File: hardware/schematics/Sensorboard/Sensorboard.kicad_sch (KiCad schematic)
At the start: 36 parts, among them J1 Grauwasser, J2 BNO055 IMU, J3 BME680 #0 Innen, J4 RS485, J5 BME680 #1 Außen, J6 HX711 GasWaage, J7 LT452 Malibu, J8 Frischwasser, U1 ESP32-S3-DevKitC, U2 TSR1-2450E, U3 MCP1700x-330xxTT, U4 SP3485CP, U5 PCF8523T, Y1 32.768

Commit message: hw(sensorboard): KiCad Schaltplan aktualisiert, Gerber + Fertigungsdaten Rev 1.0
- Sensorboard KiCad-Dateien aktualisiert (PCB, Schaltplan, Projekt)
- Autosave-/Lock-Dateien entfernt
- Gerber-Dateien für alle Layer hinzugefügt
- Fertigungspaket Rev 1.0 (BOM, Bestückung, Positionen, IPC-Netlist)
- Interactive BOM (ibom.html) hinzugefügt
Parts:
- removed U2: TSR1-2450E, Converter_DCDC:Converter_DCDC_TRACO_TSR1-xxxxE_THT, symbol Converter_DCDC:TSR1-2450E
- removed U3: MCP1700x-330xxTT, Package_TO_SOT_SMD:SOT-23, symbol Regulator_Linear:MCP1700x-330xxTT
- added D5, D6, D7: 1N4148, Diode_THT:D_DO-35_SOD27_P7.62mm_Horizontal, symbol Diode:1N4148
- added D8, D9: BZV55B3V3, Diode_SMD:D_MiniMELF, symbol Diode:BZV55B3V3
- added H1, H2, H3, H4: MountingHole_Pad, MountingHole:MountingHole_3.2mm_M3_Pad, symbol Mechanical:MountingHole_Pad
- added Q1, Q2, Q3: BSS138, Package_TO_SOT_SMD:SOT-23, symbol Transistor_FET:BSS138
- added R11, R13, R15: 100, Resistor_SMD:R_0402_1005Metric, symbol Device:R
- added R12, R14, R16, R17, R19: 100k, Resistor_SMD:R_0402_1005Metric, symbol Device:R
- added R18, R20: 22k, Resistor_SMD:R_0402_1005Metric, symbol Device:R
- added TP1: USB PWR, Connector_PinHeader_2.54mm:PinHeader_1x02_P2.54mm_Vertical, symbol Connector:TestPoint_2Pole
- added U2: TSR2-2450, Converter_DCDC:Converter_DCDC_TRACO_TSR2-xxxx_THT, symbol Converter_DCDC:TSR2-2450
- added U3: LDL1117S33R, Package_TO_SOT_SMD:SOT-223-3_TabPin2, symbol Regulator_Linear:AMS1117-3.3
- C1, C2: footprint (none) -> Capacitor_THT:CP_Radial_D5.0mm_P2.50mm
- C3, C4: value 1uF -> 10uF; footprint (none) -> Capacitor_SMD:C_0402_1005Metric
- C5, C6: footprint (none) -> Capacitor_SMD:C_0402_1005Metric
- J1, J8: footprint (none) -> Connector_JST:JST_XH_B3B-XH-A_1x03_P2.50mm_Vertical
- NT1: footprint (none) -> NetTie:NetTie-2_SMD_Pad0.5mm
- R1, R10, R2, R3, R4, R5, R6, R7, R8, R9: footprint (none) -> Resistor_SMD:R_0402_1005Metric
- Y1: footprint (none) -> Crystal:Crystal_SMD_3215-2Pin_3.2x1.5mm
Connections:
- net +3.3V: now also U3.2 (VO)
- net +5V: now also U2.3 (Vout), U3.3 (VI)
- net 12V - AUS: now also D6.2 (A), Q2.3 (D)
- net 12V - EIN: now also D5.2 (A), Q1.3 (D)
- net GND: now also D8.2 (A), D9.2 (A), H1.1, H2.1, H3.1, H4.1, Q1.2 (S), Q2.2 (S), Q3.2 (S), R12.1, R14.1, R16.1, R18.2, R20.2, TP1.1, U2.2 (GND), U3.1 (GND)
- net Multimedia: now also D7.2 (A), Q3.3 (D)
- net SB: now also R17.1
- net at U1.17 (GPIO11/ADC2_CH0): now also R11.1
- net at U1.18 (GPIO12/ADC2_CH1): now also R13.1
- net at U1.19 (GPIO13/ADC2_CH2): now also R15.1
- net at U1.4 (GPIO4/ADC1_CH3): now also D8.1 (K), R17.2, R18.1
- net at U1.5 (GPIO5/ADC1_CH4): now also D9.1 (K), R19.2, R20.1
- net +12V renamed WB
- net WB: now also D5.1 (K), D6.1 (K), D7.1 (K), R19.1, TP1.2, U2.1 (Vin)
- new net: Q2.1 (G), R13.2, R14.2
- new net: Q1.1 (G), R11.2, R12.2
- new net: Q3.1 (G), R15.2, R16.2
- no-connect marks 4 -> 27
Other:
- moved on the sheet: D4

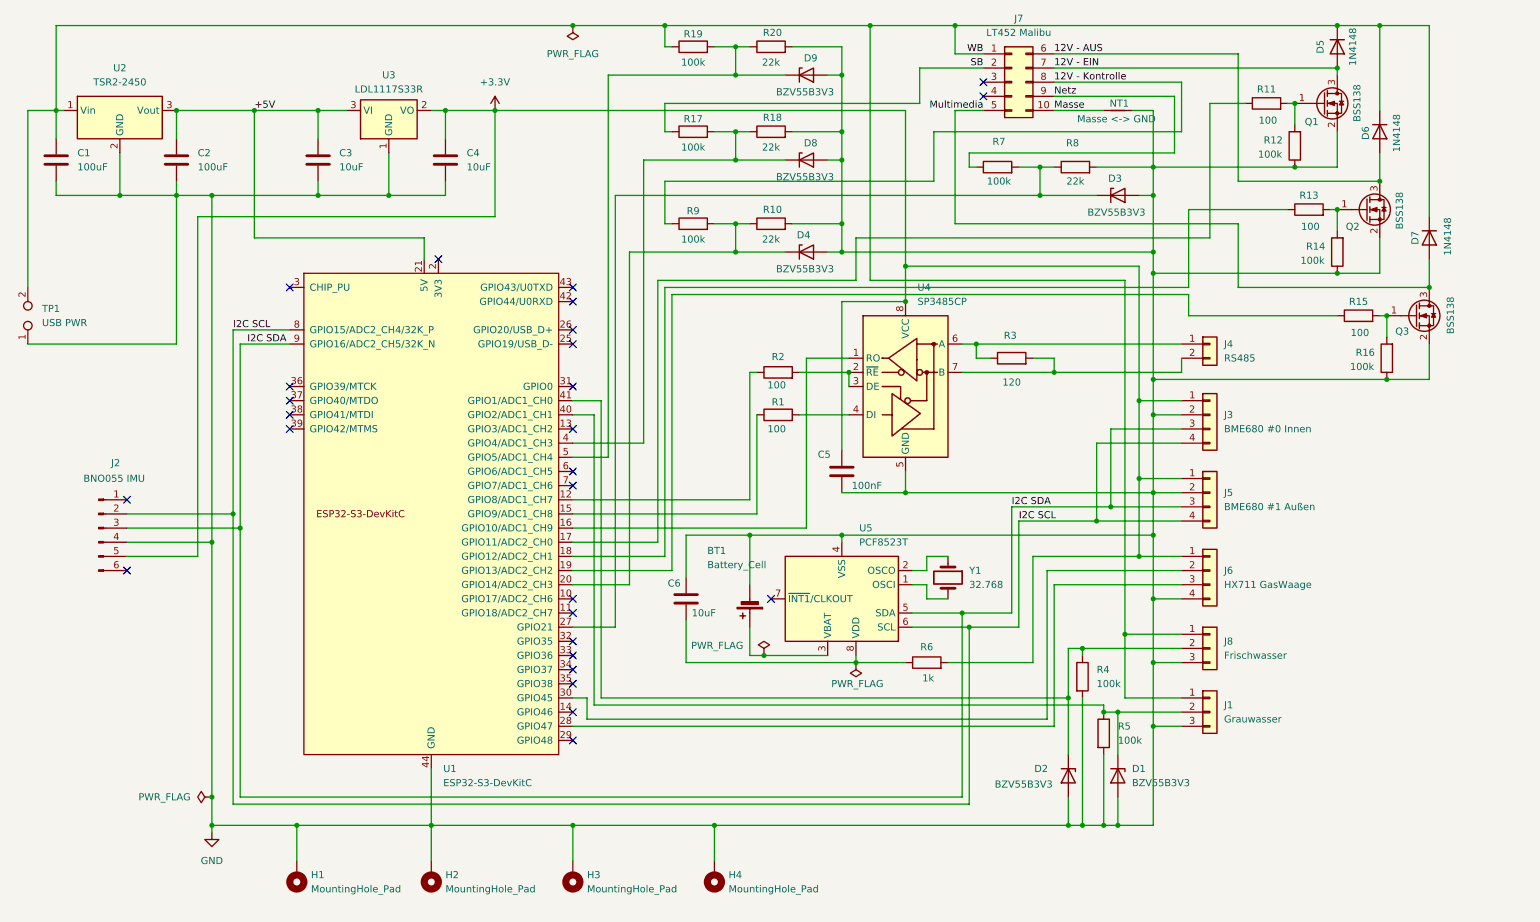
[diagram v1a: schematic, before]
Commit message: hw(sensorboard): KiCad Schaltplan + Gerber aktualisiert
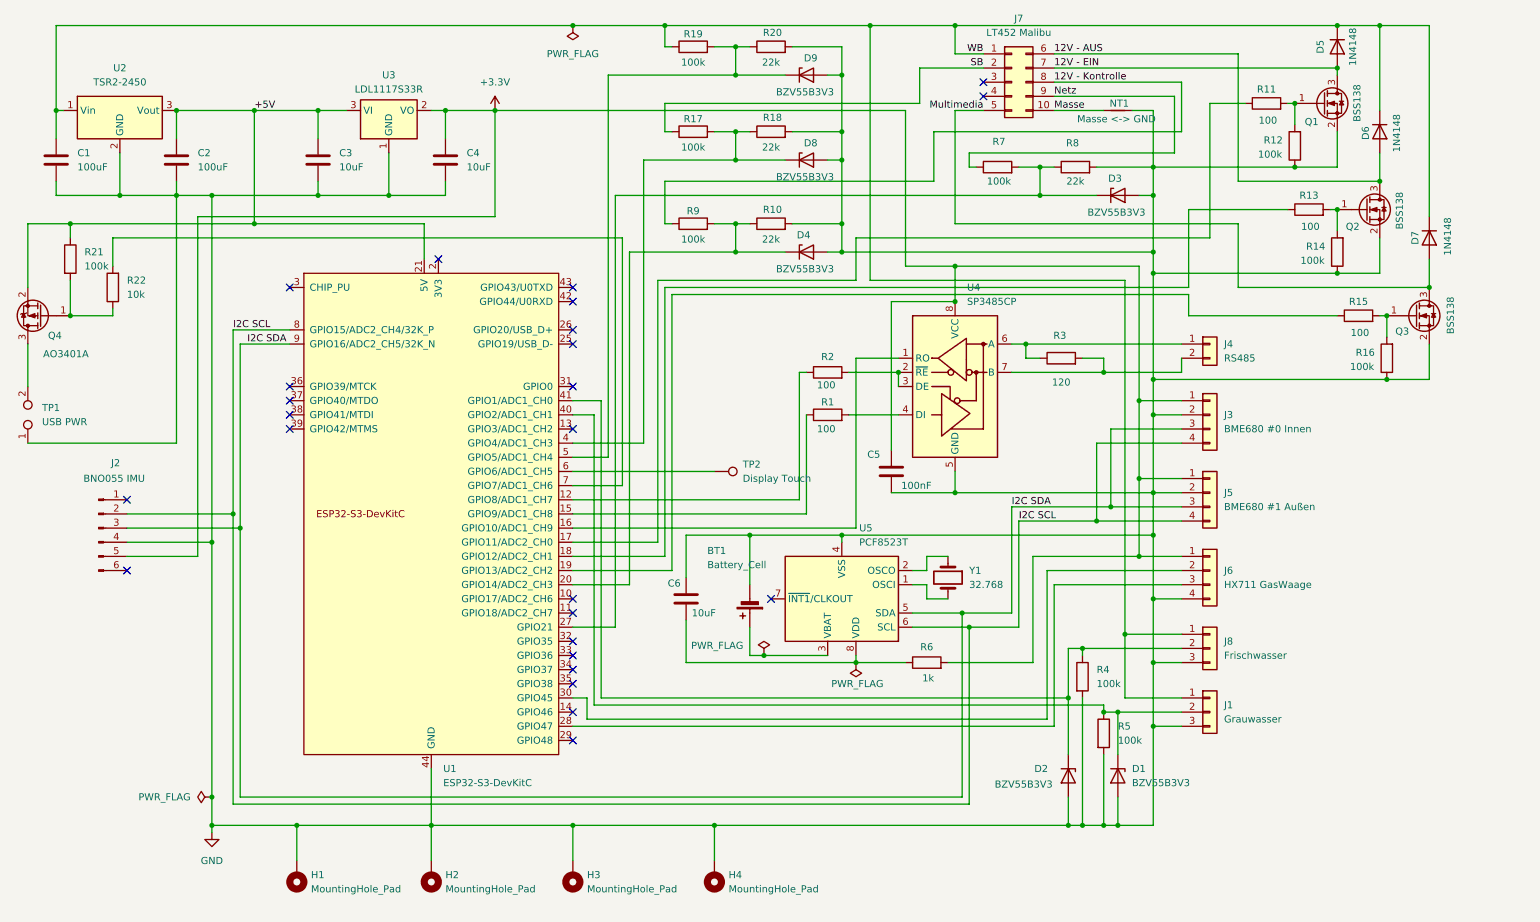
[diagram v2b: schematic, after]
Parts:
- added Q4: AO3401A, Package_TO_SOT_SMD:SOT-23, symbol Transistor_FET:AO3401A
- added R21: 100k, Resistor_SMD:R_0402_1005Metric, symbol Device:R
- added R22: 10k, Resistor_SMD:R_0402_1005Metric, symbol Device:R
- added TP2: Display Touch, TestPoint:TestPoint_THTPad_1.0x1.0mm_Drill0.5mm, symbol Connector:TestPoint
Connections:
- net +5V: now also Q4.2 (S), R21.1
- net WB: no longer TP1.2
- net at U1.6 (GPIO6/ADC1_CH5): now also TP2.1
- net at U1.7 (GPIO7/ADC1_CH6): now also R22.2
- new net: Q4.1 (G), R21.2, R22.1
- new net: Q4.3 (D), TP1.2
- no-connect marks 27 -> 25
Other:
- moved on the sheet: C5, R1, R2, R3, TP1, U4

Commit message: hardware(kicad): Sensorboard Rev 1.0 – Schematic/PCB aktualisiert, Produktionsdateien aus Tracking entfernt
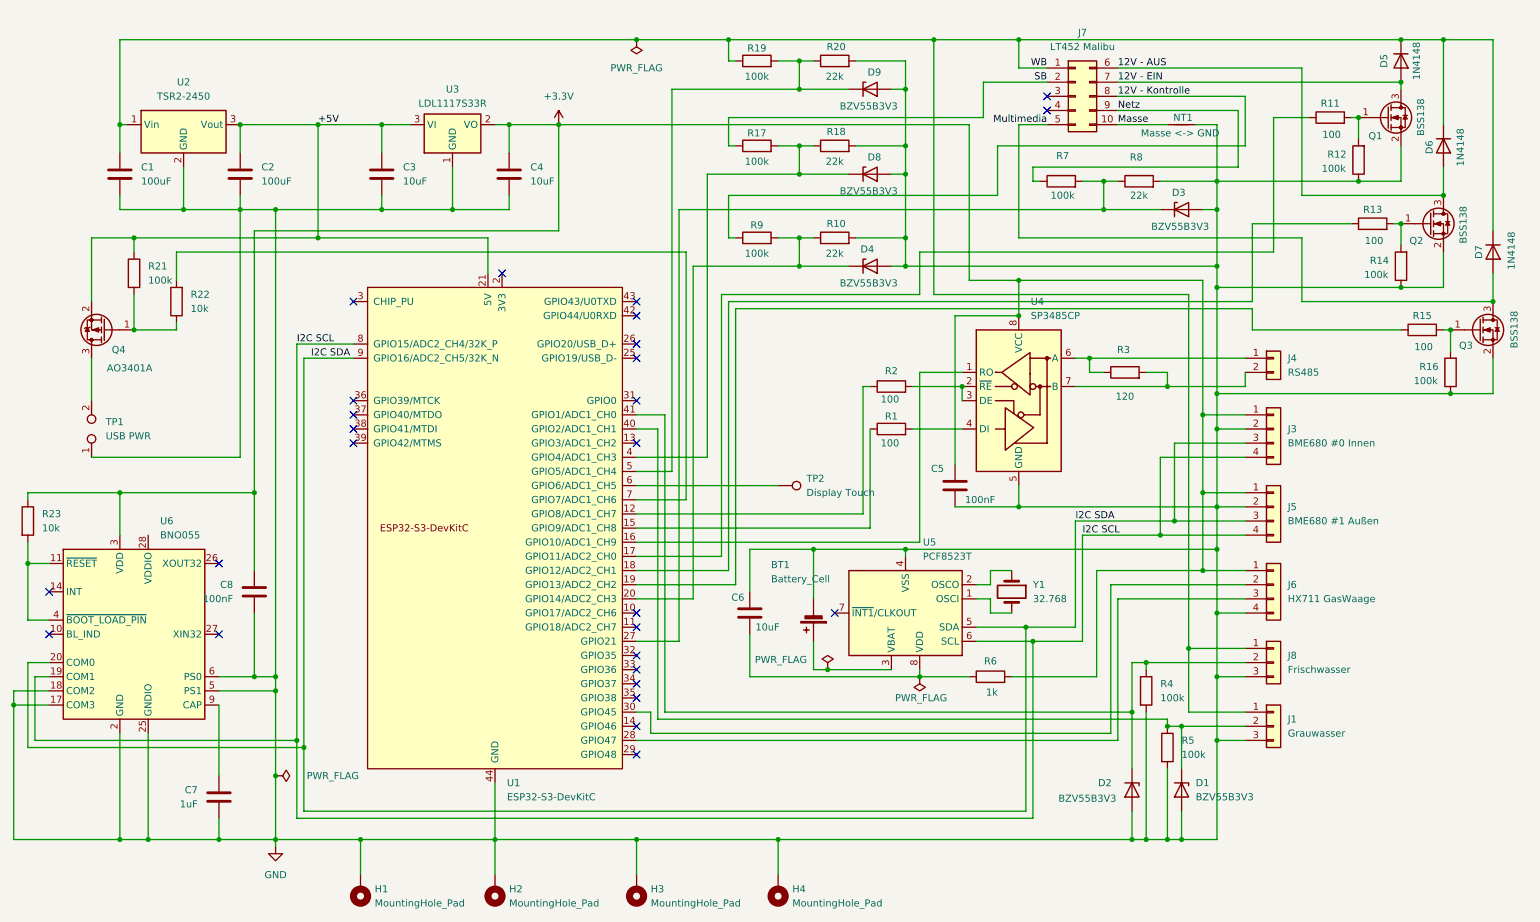
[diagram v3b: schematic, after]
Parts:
- removed J2: BNO055 IMU, Connector_PinHeader_2.54mm:PinHeader_1x06_P2.54mm_Vertical, symbol Connector:Conn_01x06_Pin
- added C7: 1uF, Capacitor_SMD:C_0402_1005Metric, symbol Device:C
- added C8: 100nF, Capacitor_SMD:C_0402_1005Metric, symbol Device:C
- added R23: 10k, Resistor_SMD:R_0402_1005Metric, symbol Device:R
- added U6: BNO055, Package_LGA:LGA-28_5.2x3.8mm_P0.5mm, symbol Sensor_Motion:BNO055
- BT1: footprint Battery:BatteryHolder_Keystone_3034_1x20mm -> Battery:BatteryHolder_Keystone_3000_1x12mm
- U1: footprint PCM_Espressif:ESP32-S3-DevKitC -> PCM_Espressif:ESP32-S3-DevKitC-Heemol
- U4: footprint Package_DIP:DIP-8_W7.62mm -> Package_SO:SOIC-8_3.9x4.9mm_P1.27mm
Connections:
- net +3.3V: now also C8.1, R23.1, U6.3 (VDD)
- net GND: now also C7.2, C8.2, U6.17 (COM3), U6.18 (COM2), U6.2 (GND), U6.25 (GNDIO), U6.5 (PS1), U6.6 (PS0)
- net I2C SCL: now also U6.19 (COM1)
- net I2C SDA: now also U6.20 (COM0)
- new net: R23.2, U6.11 (~{RESET}), U6.4 (~{BOOT_LOAD_PIN})
- new net: C7.1, U6.9 (CAP)
- no-connect marks 25 -> 27
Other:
- moved on the sheet: BT1, C1, C2, C3, C4, C5, C6, D1, D2, D3, D4, D5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

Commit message: hardware(sensorboard): Zwei neue 12V-Schaltausgänge (Pumpe, Licht) hinzugefügt, Aufräumen und Fehler des Vorgänger-Boards behoben
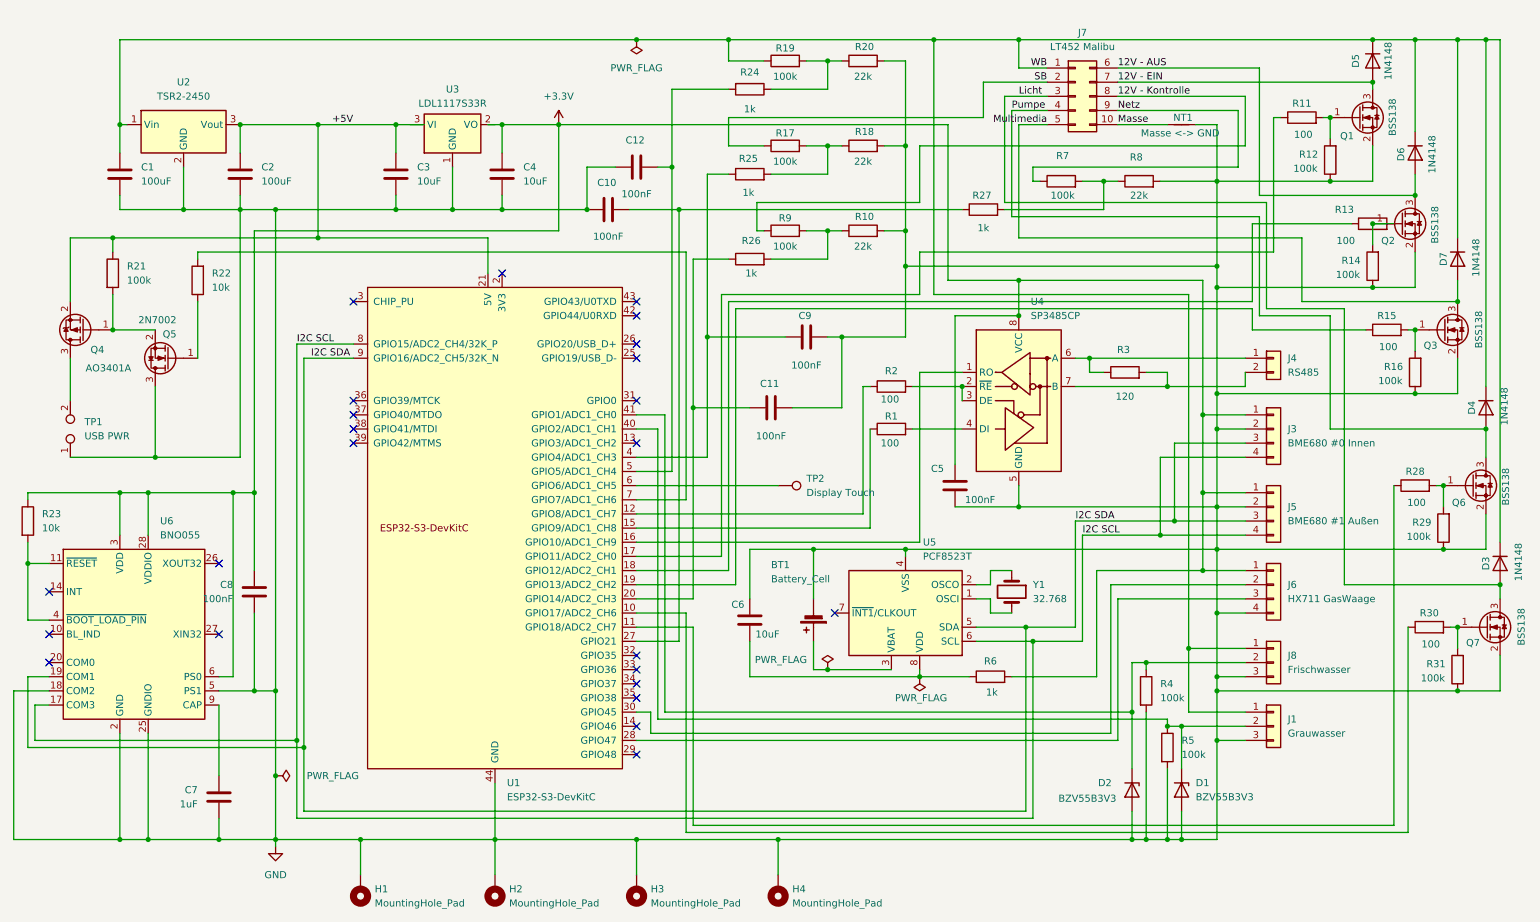
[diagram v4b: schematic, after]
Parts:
- removed D3, D4, D8, D9: BZV55B3V3, Diode_SMD:D_MiniMELF, symbol Diode:BZV55B3V3
- added C10, C11, C12, C9: 100nF, Capacitor_SMD:C_0402_1005Metric, symbol Device:C
- added D3, D4: 1N4148, Diode_THT:D_DO-35_SOD27_P7.62mm_Horizontal, symbol Diode:1N4148
- added Q5: 2N7002, Package_TO_SOT_SMD:SOT-23, symbol Transistor_FET:2N7002
- added Q6, Q7: BSS138, Package_TO_SOT_SMD:SOT-23, symbol Transistor_FET:BSS138
- added R24, R25, R26, R27: 1k, Resistor_SMD:R_0402_1005Metric, symbol Device:R
- added R28, R30: 100, Resistor_SMD:R_0402_1005Metric, symbol Device:R
- added R29, R31: 100k, Resistor_SMD:R_0402_1005Metric, symbol Device:R
- TP2: footprint TestPoint:TestPoint_THTPad_1.0x1.0mm_Drill0.5mm -> TestPoint:TestPoint_THTPad_2.0x2.0mm_Drill1.0mm
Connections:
- net +3.3V: now also U6.28 (VDDIO), U6.6 (PS0); no longer U3.2 (VO)
- net +5V: no longer U3.3 (VI)
- net GND: now also C10.2, C11.1, C12.2, C9.1, Q5.3 (D), Q6.2 (S), Q7.2 (S), R29.1, R31.1; no longer U6.17 (COM3), U6.6 (PS0)
- net I2C SCL: now also U6.17 (COM3); no longer U6.19 (COM1)
- net I2C SDA: now also U6.19 (COM1); no longer U6.20 (COM0)
- net WB: now also D3.1 (K), D4.1 (K)
- net at R7.2, R8.1: now also R27.2; no longer U1.27 (GPIO21)
- net at Q4.1 (G), R21.2: now also Q5.2 (S); no longer R22.1
- net at R19.2, R20.1: now also R24.1; no longer U1.5 (GPIO5/ADC1_CH4)
- net at R10.1, R9.2: now also R26.2; no longer U1.20 (GPIO14/ADC2_CH3)
- net Licht: now reaches J7.3 (Pin_3)
- net Licht: now also D3.2 (A), Q7.3 (D)
- net Pumpe: now reaches J7.4 (Pin_4)
- net Pumpe: now also D4.2 (A), Q6.3 (D)
- net at R17.2, R18.1: now also R25.2; no longer U1.4 (GPIO4/ADC1_CH3)
- net at U1.10 (GPIO17/ADC2_CH6): now also R30.1
- net at U1.11 (GPIO18/ADC2_CH7): now also R28.1
- new net: Q6.1 (G), R28.2, R29.2
- new net: C12.1, R24.2, U1.5 (GPIO5/ADC1_CH4)
- new net: C10.1, R27.1, U1.27 (GPIO21)
- new net: C11.2, R26.1, U1.20 (GPIO14/ADC2_CH3)
- new net: Q5.1 (G), R22.1
- new net: Q7.1 (G), R30.2, R31.2
- new net: C9.2, R25.1, U1.4 (GPIO4/ADC1_CH3)
- no-connect marks 27 -> 24
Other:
- company: (none) -> Hajo Harms / WoMoHome
- moved on the sheet: C3, C4, C6, D5, D6, D7, Q1, Q2, Q3, Q4, R10, R11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
